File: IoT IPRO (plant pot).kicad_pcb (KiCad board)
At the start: 2 copper layers, 110.5 x 52.1 mm, 13 parts, among them J1 Barrel_Jack, U1 DS18S20

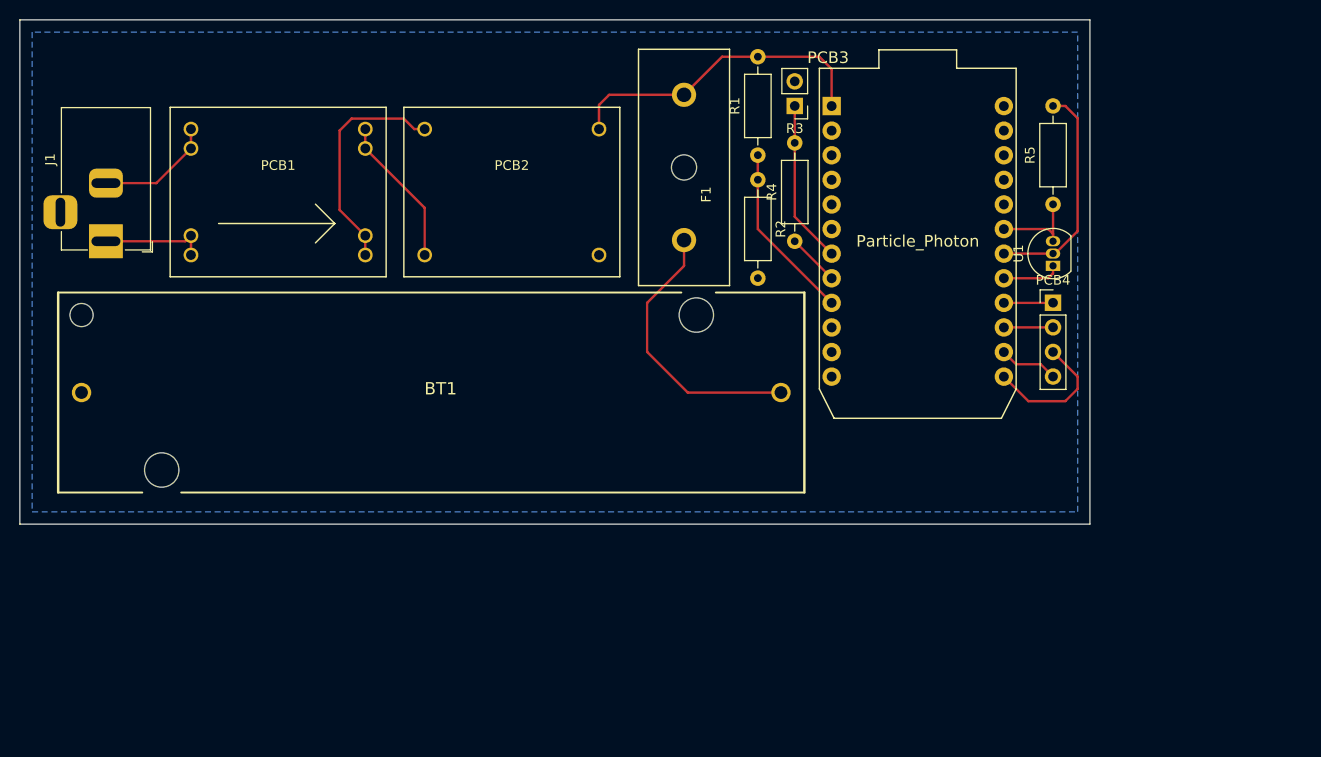
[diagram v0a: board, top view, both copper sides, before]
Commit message: Redo PCB. Tracks too thin right now
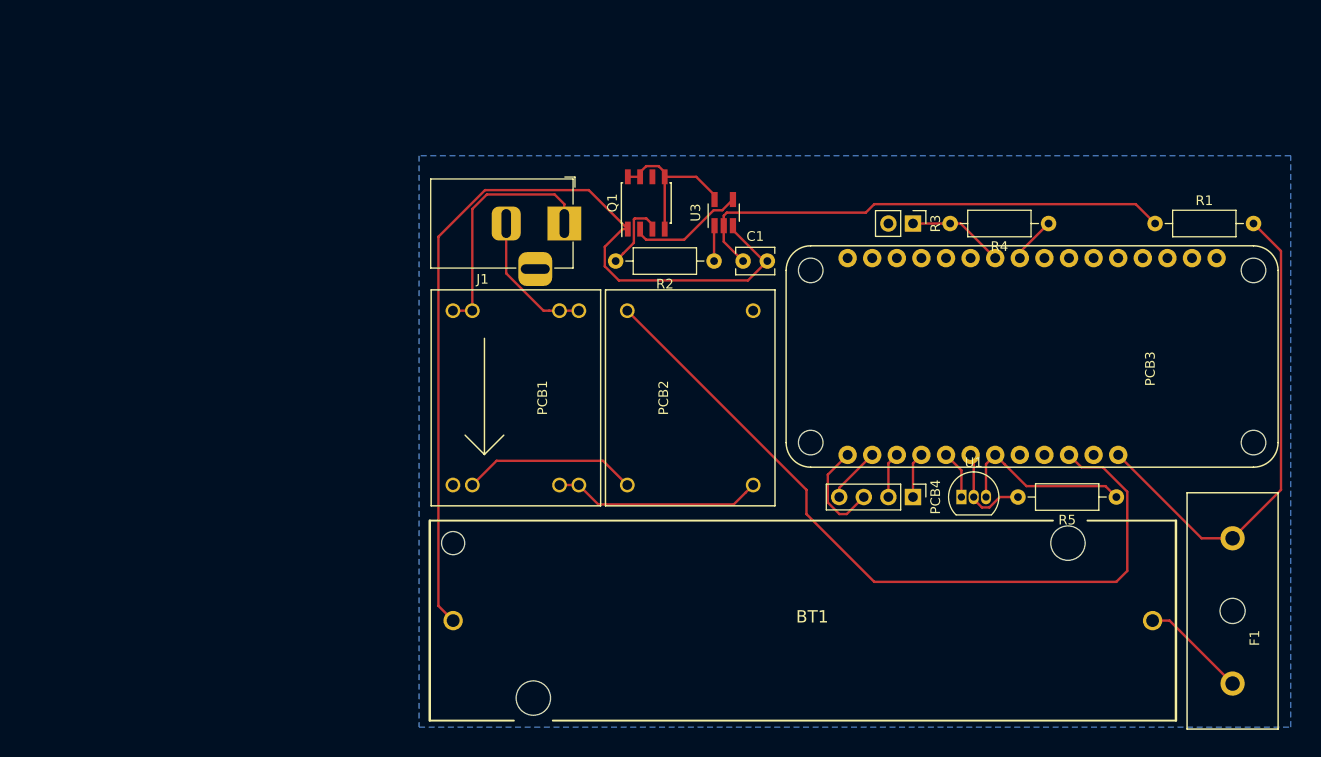
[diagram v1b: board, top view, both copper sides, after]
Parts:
- added C1: 100nF, Capacitor_THT:C_Disc_D3.8mm_W2.6mm_P2.50mm, F.Cu at (92.5, 38.9)
- added Q1: Q_DUAL_NMOS_S1G1S2G2D1D1D2D2, Package_SO:SOIC-8_3.9x4.9mm_P1.27mm, F.Cu at (82.5, 32.9)
- added U3: AP9101C-SOT25, Package_TO_SOT_SMD:SOT-23-5_HandSoldering, F.Cu at (90.5, 33.9)
- PCB3: value Particle_Photon -> Particle_Argon; footprint IPRO_smart_pot:photon_tht -> IPRO_smart_pot:argon_tht
- R1: value 100K -> 330
- R2: value 100K -> 2.7k
- moved F1 72.8 mm to (143.0, 75.0)
- moved J1 47.4 mm to (74.0, 35.0), turned to 0 degrees
- moved BT1 45.0 mm to (126.0, 68.0)
- moved R1 41.6 mm to (135.0, 35.0), turned to 0 degrees
- moved PCB1 32.5 mm to (69.0, 53.0), turned to 270 degrees
- moved R5 30.9 mm to (131.0, 63.2), turned to 180 degrees
- moved PCB2 28.1 mm to (87.0, 53.0), turned to 90 degrees
- moved PCB3 27.8 mm to (135.0, 50.0), turned to 270 degrees
- moved R4 26.3 mm to (124.0, 35.0), turned to 180 degrees
- moved U1 25.7 mm to (115.0, 63.2), turned to 0 degrees
- moved PCB4 24.7 mm to (110.0, 63.2), turned to 270 degrees
- moved R3 17.2 mm to (110.0, 35.0), turned to 270 degrees
- moved R2 9.53 mm to (89.5, 38.9), turned to 180 degrees
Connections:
- BT1 pad 2: GND -> Net-(BT1-Pad2)
- F1 pad 1: +5V -> +BATT
- PCB2 pad 4: +5V -> Net-(PCB2-Pad4)
- PCB3 pad 1: +5V -> (no net)
- PCB3 pad 11: Net-(PCB3-Pad11) -> (no net)
- PCB3 pad 12: Net-(PCB3-Pad12) -> (no net)
- PCB3 pad 13: Net-(PCB3-Pad13) -> (no net)
- PCB3 pad 14: Net-(PCB3-Pad14) -> (no net)
- PCB3 pad 15: Net-(PCB3-Pad15) -> (no net)
- PCB3 pad 16: Net-(PCB3-Pad16) -> (no net)
- PCB3 pad 2: GND -> (no net)
- PCB3 pad 24: Net-(PCB3-Pad24) -> (no net)
- PCB3 pad 3: Net-(PCB3-Pad3) -> (no net)
- PCB3 pad 4: Net-(PCB3-Pad4) -> GND
- PCB3 pad 5: Net-(PCB3-Pad5) -> (no net)
- PCB3 pad 6: Net-(PCB3-Pad6) -> (no net)
- PCB3 pad 7: Net-(PCB3-Pad7) -> (no net)
- PCB3 pad 8: Net-(PCB3-Pad8) -> (no net)
- PCB4 pad 1: Net-(PCB3-Pad16) -> Net-(PCB3-Pad20)
- PCB4 pad 2: Net-(PCB3-Pad15) -> Net-(PCB3-Pad19)
- PCB4 pad 3: Net-(PCB3-Pad13) -> Net-(PCB3-Pad17)
- PCB4 pad 4: Net-(PCB3-Pad14) -> Net-(PCB3-Pad18)
- R1 pad 1: Net-(PCB3-Pad9) -> Net-(C1-Pad1)
- R1 pad 2: +5V -> +BATT
- R2 pad 1: Net-(PCB3-Pad9) -> Net-(R2-Pad1)
- R3 pad 1: Net-(PCB3-Pad7) -> Net-(PCB3-Pad10)
- R4 pad 1: Net-(PCB3-Pad8) -> Net-(PCB3-Pad9)
- R4 pad 2: Net-(PCB3-Pad7) -> Net-(PCB3-Pad10)
- R5 pad 1: Net-(PCB3-Pad19) -> Net-(PCB3-Pad23)
- R5 pad 2: Net-(PCB3-Pad18) -> Net-(PCB3-Pad22)
- U1 pad 1: Net-(PCB3-Pad17) -> Net-(PCB3-Pad21)
- U1 pad 2: Net-(PCB3-Pad18) -> Net-(PCB3-Pad22)
- U1 pad 3: Net-(PCB3-Pad19) -> Net-(PCB3-Pad23)
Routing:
- net Net-(BT1-Pad2): track 0.00 -> 92.2 mm
- net Net-(PCB2-Pad4): track 0.00 -> 80.9 mm
- net Net-(C1-Pad1): track 0.00 -> 51.4 mm
- net +BATT: track 0.00 -> 51.1 mm
- net +5V: track 32.9 -> 0.00 mm
- net Net-(PCB3-Pad23): track 0.00 -> 19.1 mm
- net Net-(BT1-Pad1): track 28.7 -> 11.0 mm
- net Net-(PCB3-Pad18): track 23.3 -> 5.76 mm
- net Net-(Q1-Pad4): track 0.00 -> 17.1 mm
- net Net-(PCB3-Pad7): track 16.8 -> 0.00 mm
- net Net-(PCB3-Pad13): track 14.1 -> 0.00 mm
- net Net-(J1-Pad1): track 11.0 -> 25.0 mm
- net Net-(PCB3-Pad9): track 18.4 -> 4.80 mm
- net Net-(Q1-Pad2): track 0.00 -> 12.0 mm
- net Net-(PCB3-Pad22): track 0.00 -> 10.1 mm
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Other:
- board outline removed

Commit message: Adjust trace widths
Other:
- net class Power added: clearance 0.2, trace_width 0.8, via_dia 0.8, via_drill 0.4
- net class Signal added: clearance 0.2, trace_width 0.25, via_dia 0.8, via_drill 0.4
- rule trace_min: 0.25 -> 0.127
- rule via_min_size: 0.4 -> 0.6
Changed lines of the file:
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@@
     (zone_clearance 0.508)
     (zone_45_only yes)
-    (trace_min 0.25)
+    (trace_min 0.127)
     (segment_width 0.2)
     (edge_width 0.1)
     (via_size 0.8)
     (via_drill 0.4)
-    (via_min_size 0.4)
+    (via_min_size 0.6)
     (via_min_drill 0.3)
     (uvia_size 0.3)
@@
     (uvia_dia 0.3)
     (uvia_drill 0.1)
+    (add_net "Net-(PCB3-Pad10)")
+    (add_net "Net-(PCB3-Pad17)")
+    (add_net "Net-(PCB3-Pad18)")
+    (add_net "Net-(PCB3-Pad19)")
+    (add_net "Net-(PCB3-Pad20)")
+    (add_net "Net-(PCB3-Pad21)")
+    (add_net "Net-(PCB3-Pad22)")
+    (add_net "Net-(PCB3-Pad23)")
+    (add_net "Net-(PCB3-Pad9)")
+  )
+  (net_class Power ""
+    (clearance 0.2)
+    (trace_width 0.8)
+    (via_dia 0.8)
+    (via_drill 0.4)
+    (uvia_dia 0.3)
+    (uvia_drill 0.1)
     (add_net +BATT)
     (add_net GND)
@@
     (add_net "Net-(PCB1-Pad4)")
     (add_net "Net-(PCB2-Pad4)")
-    (add_net "Net-(PCB3-Pad10)")
-    (add_net "Net-(PCB3-Pad17)")
-    (add_net "Net-(PCB3-Pad18)")
-    (add_net "Net-(PCB3-Pad19)")
-    (add_net "Net-(PCB3-Pad20)")
-    (add_net "Net-(PCB3-Pad21)")
-    (add_net "Net-(PCB3-Pad22)")
-    (add_net "Net-(PCB3-Pad23)")
-    (add_net "Net-(PCB3-Pad9)")
     (add_net "Net-(Q1-Pad2)")
     (add_net "Net-(Q1-Pad4)")
     (add_net "Net-(R2-Pad1)")
   )
+  (net_class Signal ""
+    (clearance 0.2)
+    (trace_width 0.25)
+    (via_dia 0.8)
+    (via_drill 0.4)
+    (uvia_dia 0.3)
+    (uvia_drill 0.1)
+  )
   (module Resistor_THT:R_Axial_DIN0207_L6.3mm_D2.5mm_P10.16mm_Horizontal (layer F.Cu)

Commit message: Update PCB, PDFs
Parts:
- moved C1 1.00 mm to (92.5, 39.9)
- moved Q1 1.00 mm to (82.5, 33.9)
- moved R2 1.00 mm to (89.5, 39.9)
- moved U3 1.00 mm to (90.5, 34.9)
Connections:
- Q1 pad 5: Net-(Q1-Pad4) -> Net-(Q1-Pad5)
- Q1 pad 6: (no net) -> Net-(Q1-Pad5)
- Q1 pad 7: Net-(Q1-Pad4) -> Net-(Q1-Pad5)
- Q1 pad 8: Net-(Q1-Pad4) -> Net-(Q1-Pad5)
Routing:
- net Net-(BT1-Pad2): track 92.2 -> 73.5 mm
- net Net-(Q1-Pad4): track 17.1 -> 6.69 mm
- net Net-(Q1-Pad5): track 0.00 -> 3.81 mm
- net Net-(PCB2-Pad4): track 80.9 -> 78.2 mm
- net Net-(J1-Pad1): track 25.0 -> 22.5 mm
- net Net-(PCB1-Pad3): track 18.1 -> 20.1 mm
- net GND: track 7.78 -> 6.08 mm
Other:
- board outline added: 92 x 59 mm

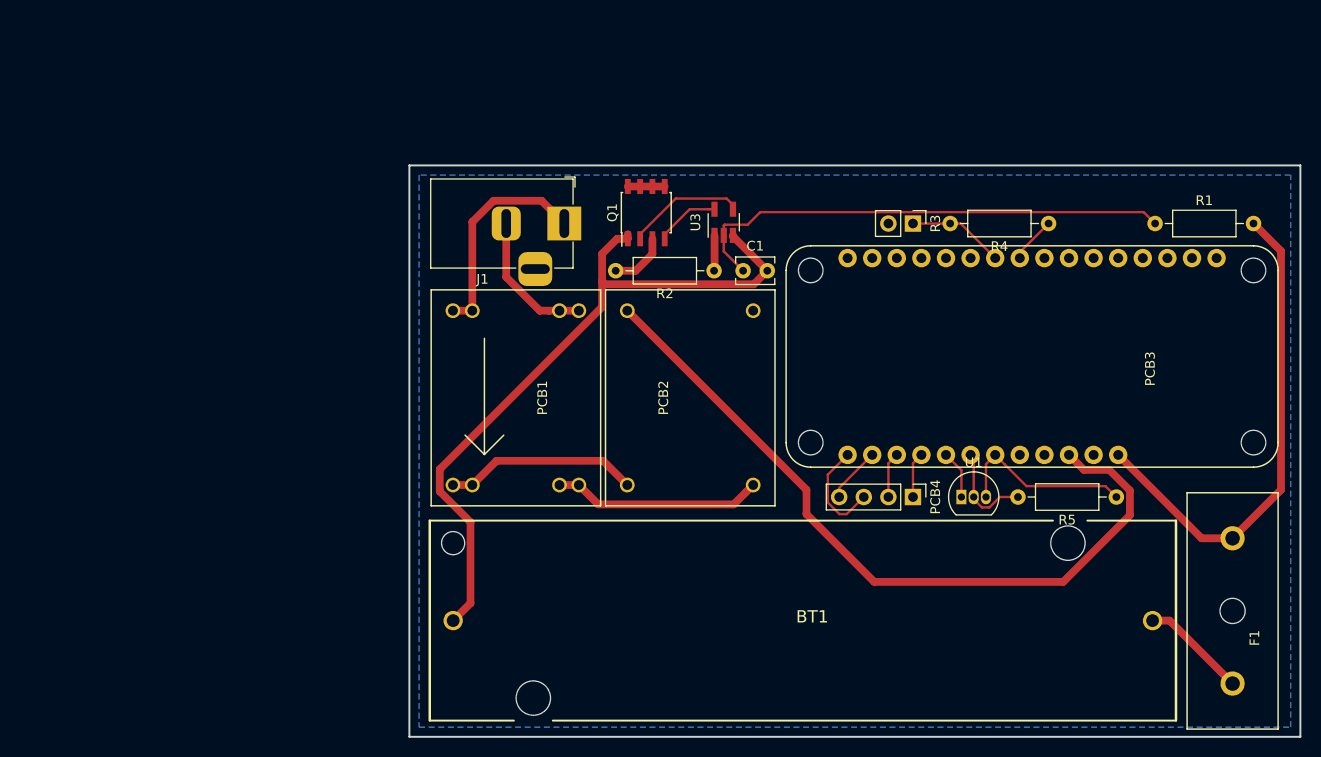
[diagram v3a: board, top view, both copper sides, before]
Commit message: Redo board layout
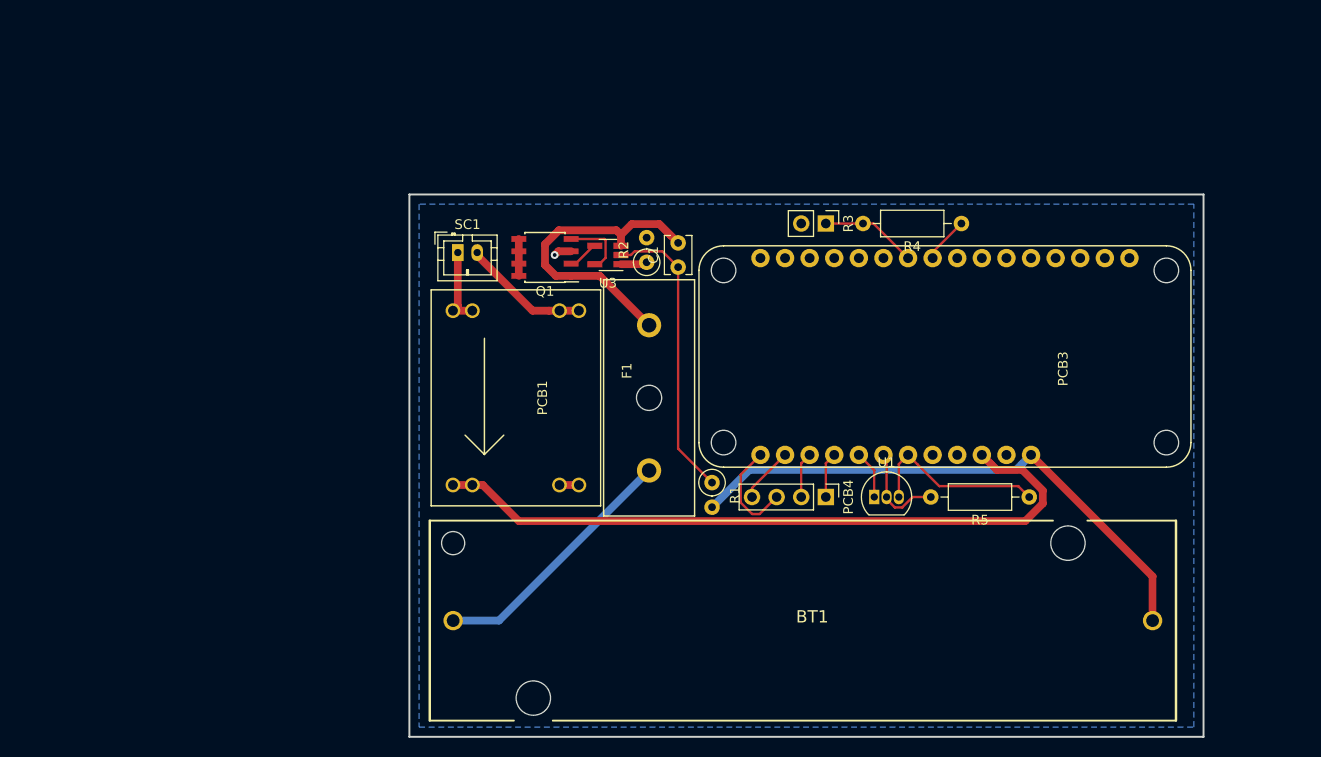
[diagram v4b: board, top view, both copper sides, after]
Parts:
- removed J1: Barrel_Jack, Connector_BarrelJack:BarrelJack_Horizontal
- removed PCB2: TP4056_board, IPRO_smart_pot:TP4056_board
- added SC1: Solar_Cells, Connector_JST:JST_PH_B2B-PH-K_1x02_P2.00mm_Vertical, F.Cu at (63.0, 38.0)
- R1, R2: footprint Resistor_THT:R_Axial_DIN0207_L6.3mm_D2.5mm_P10.16mm_Horizontal -> Resistor_THT:R_Axial_DIN0207_L6.3mm_D2.5mm_P2.54mm_Vertical
- moved F1 64.1 mm to (82.8, 53.0), turned to 90 degrees
- moved R1 53.0 mm to (89.2, 61.8), turned to 270 degrees
- moved U3 12.4 mm to (78.5, 38.2), turned to 180 degrees
- moved Q1 11.4 mm to (72.0, 38.5), turned to 180 degrees
- moved PCB3 9.00 mm to (126.0, 50.0)
- moved PCB4 9.00 mm to (101.0, 63.2)
- moved R3 9.00 mm to (101.0, 35.0)
- moved R4 9.00 mm to (115.0, 35.0)
- moved R5 9.00 mm to (122.0, 63.2)
- moved U1 9.00 mm to (106.0, 63.2)
- moved R2 7.01 mm to (82.5, 39.0), turned to 90 degrees
- moved C1 6.72 mm to (85.8, 39.5), turned to 90 degrees
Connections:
- BT1 pad 1: Net-(BT1-Pad1) -> +BATT
- C1 pad 2: Net-(BT1-Pad2) -> Net-(C1-Pad2)
- F1 pad 1: +BATT -> Net-(BT1-Pad2)
- F1 pad 2: Net-(BT1-Pad1) -> Net-(C1-Pad2)
- PCB1 pad 3: Net-(PCB1-Pad3) -> +5V
- PCB1 pad 4: Net-(PCB1-Pad4) -> GND
- PCB3 pad 1: (no net) -> Net-(PCB3-Pad1)
- PCB3 pad 11: (no net) -> Net-(PCB3-Pad11)
- PCB3 pad 12: (no net) -> Net-(PCB3-Pad12)
- PCB3 pad 13: (no net) -> Net-(PCB3-Pad13)
- PCB3 pad 14: (no net) -> Net-(PCB3-Pad14)
- PCB3 pad 15: (no net) -> Net-(PCB3-Pad15)
- PCB3 pad 16: (no net) -> Net-(PCB3-Pad16)
- PCB3 pad 2: (no net) -> Net-(PCB3-Pad2)
- PCB3 pad 24: (no net) -> Net-(PCB3-Pad24)
- PCB3 pad 25: (no net) -> Net-(PCB3-Pad25)
- PCB3 pad 26: Net-(PCB2-Pad4) -> +5V
- PCB3 pad 27: (no net) -> Net-(PCB3-Pad27)
- PCB3 pad 3: (no net) -> Net-(PCB3-Pad3)
- PCB3 pad 5: (no net) -> Net-(PCB3-Pad5)
- PCB3 pad 6: (no net) -> Net-(PCB3-Pad6)
- PCB3 pad 7: (no net) -> Net-(PCB3-Pad7)
- PCB3 pad 8: (no net) -> Net-(PCB3-Pad8)
- Q1 pad 1: Net-(BT1-Pad2) -> Net-(C1-Pad2)
- U3 pad 3: Net-(BT1-Pad2) -> Net-(C1-Pad2)
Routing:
- net Net-(PCB2-Pad4): track 78.2 -> 0.00 mm
- net +5V: track 0.00 -> 72.4 mm
- net Net-(BT1-Pad2): track 73.5 -> 26.7 mm
- net Net-(C1-Pad2): track 0.00 -> 32.4 mm
- net Net-(PCB1-Pad4): track 21.7 -> 0.00 mm
- net Net-(C1-Pad1): track 51.1 -> 30.4 mm
- net Net-(PCB1-Pad3): track 20.1 -> 0.00 mm
- net Net-(PCB1-Pad2): track 22.5 -> 8.21 mm
- net Net-(BT1-Pad1): track 11.0 -> 0.00 mm
- net Net-(Q1-Pad2): track 12.3 -> 3.21 mm
- net +BATT: track 51.1 -> 57.5 mm
- net GND: track 6.08 -> 3.86 mm, vias 0 -> 1
- net Net-(PCB1-Pad1): track 14.5 -> 13.1 mm
- net Net-(R2-Pad1): track 3.67 -> 2.73 mm
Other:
- board size 92 x 59 mm -> 82 x 56 mm
